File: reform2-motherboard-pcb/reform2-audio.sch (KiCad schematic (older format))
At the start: 53 parts, among them J16 LINE_IN, J21 Conn_01x04, J7 SJ-43516-SMT, U3 WM8960

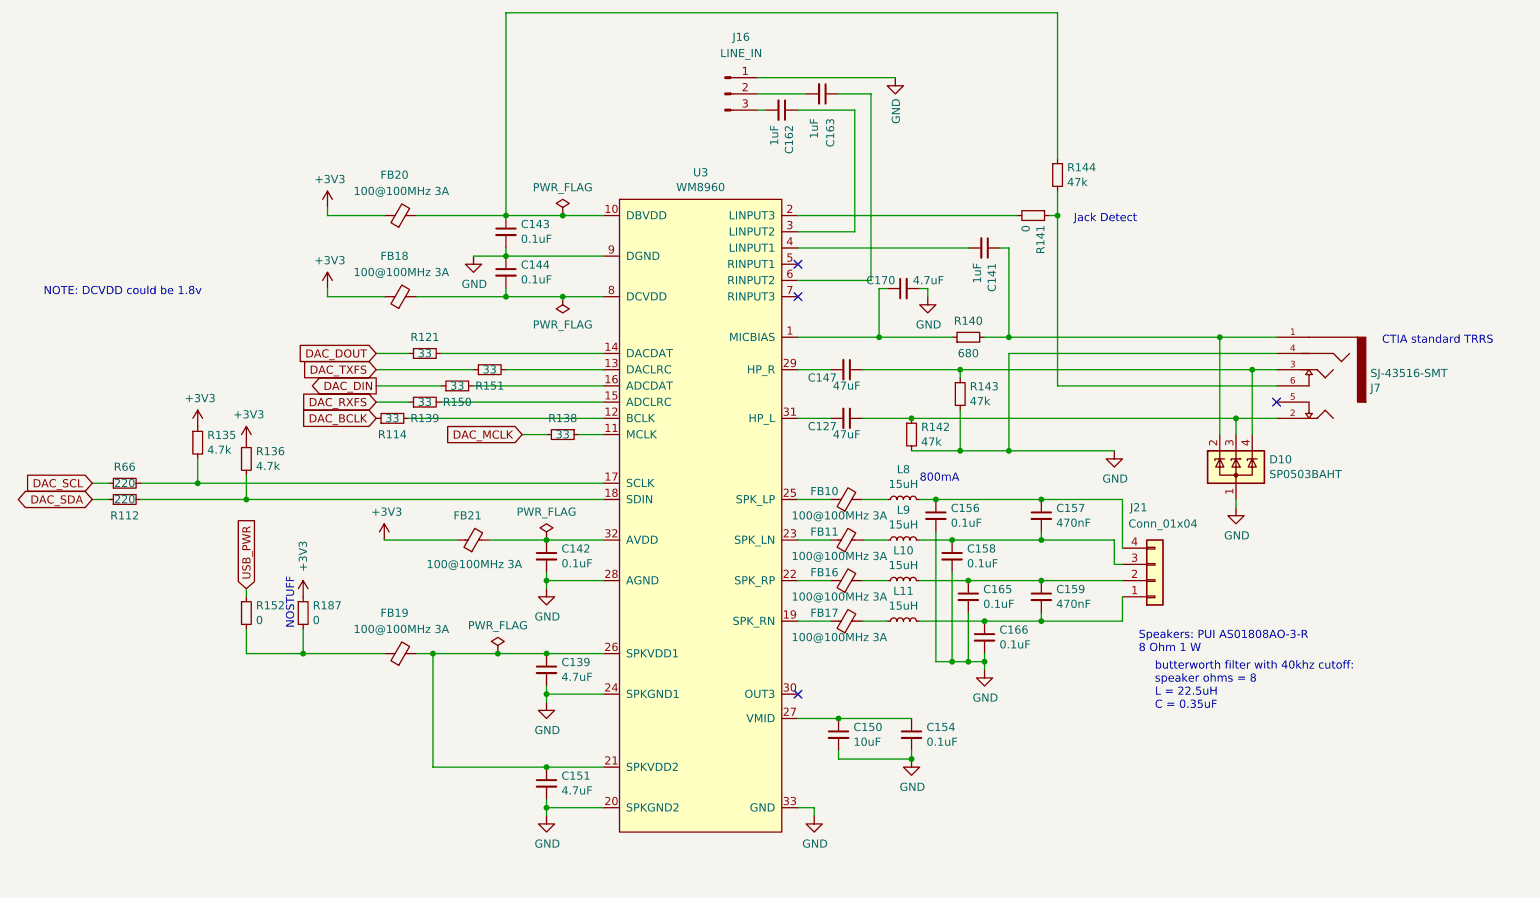
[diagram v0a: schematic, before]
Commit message: motherboard: add the split-up and cleaned up schematics that were made for the book
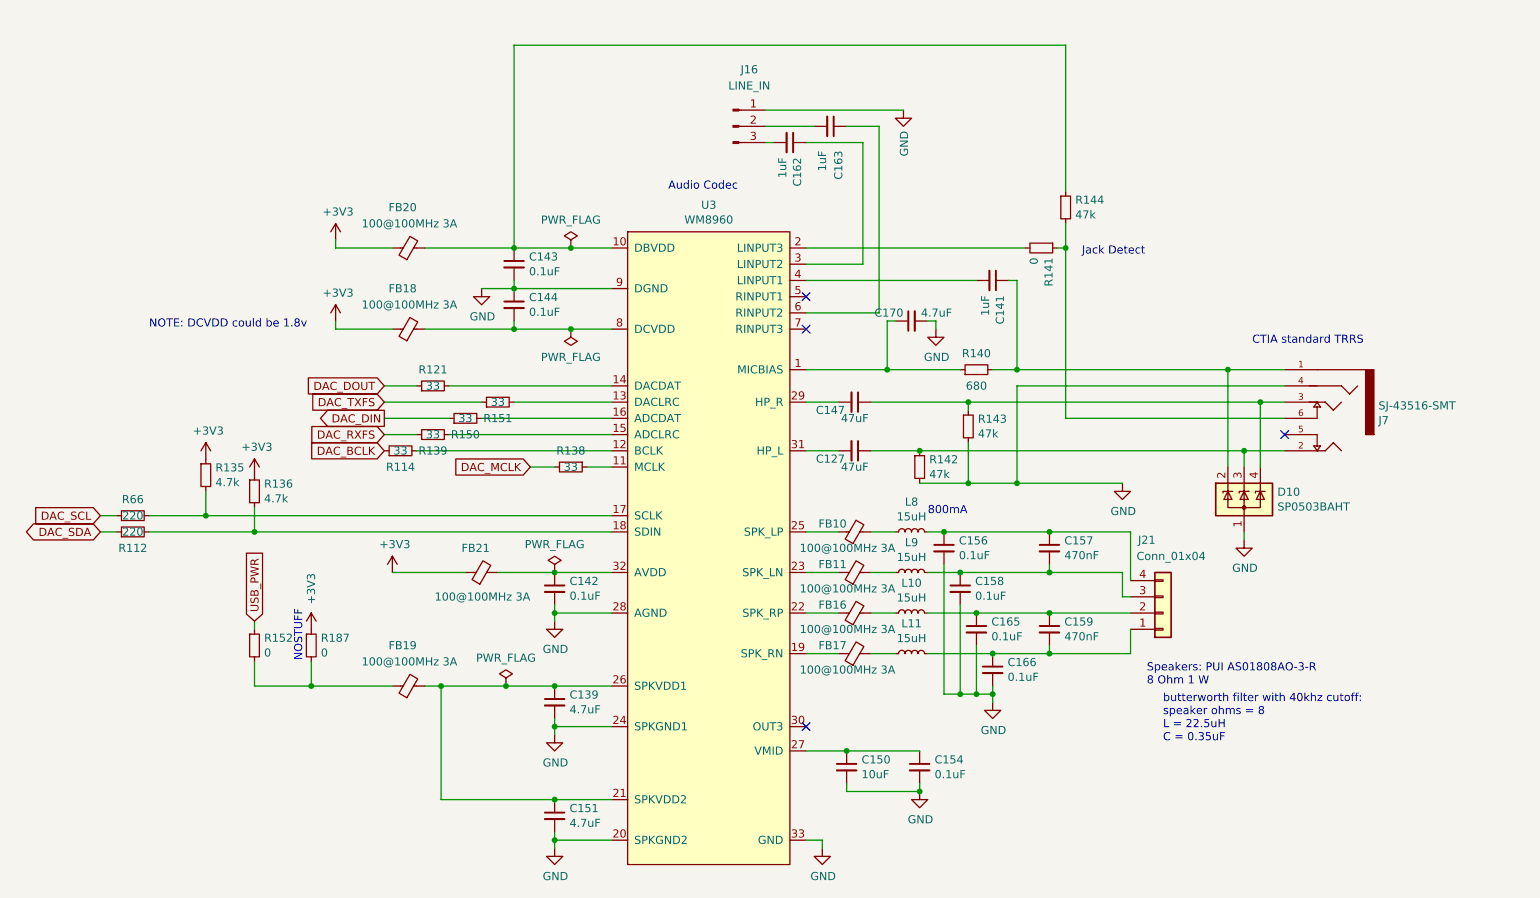
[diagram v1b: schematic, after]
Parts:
- J16, R152: DNP y -> (none)
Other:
- note added: "Audio Codec"
- moved on the sheet: C127, C139, C141, C142, C143, C144, C147, C150, C151, C154, C156, C157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
